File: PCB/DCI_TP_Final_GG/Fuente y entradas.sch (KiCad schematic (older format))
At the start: 0 parts

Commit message: Agrego esquematico de fuente (falta completar)
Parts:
- added C?: 47uF x 35V, symbol Device:CP
- added C? (x2): C, symbol Device:C
- added D?: LED, symbol Device:LED
- added J? (x2): Conn_01x02, symbol Connector_Generic:Conn_01x02
- added J? (x2): Conn_01x10, symbol Connector_Generic:Conn_01x10
- added JP?: Jumper, symbol Device:Jumper
- added R? (x4): R, symbol Device:R
- added U?: LM317_3PinPackage, symbol Regulator_Linear:LM317_3PinPackage
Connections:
- new net: R?.1, U?.1 (ADJ)
- new net: JP?.1, R?.1, R?.2
- new net: D?.2 (A), R?.2
- new net DIR-A: J?.8 (Pin_8)
- new net DIR-B: J?.8 (Pin_8)
- new net ENA-A: J?.5 (Pin_5)
- new net ENA-B: J?.5 (Pin_5)
- new net GND: C?.2, C?.2, C?.2, D?.1 (K), J?.1 (Pin_1), J?.1 (Pin_1), J?.1 (Pin_1), J?.2 (Pin_2), JP?.2, R?.2, R?.2
- new net MS1-A: J?.7 (Pin_7)
- new net MS1-B: J?.7 (Pin_7)
- new net MS2-A: J?.6 (Pin_6)
- new net MS2-B: J?.6 (Pin_6)
- new net PFD-A: J?.2 (Pin_2)
- new net PFD-B: J?.2 (Pin_2)
- new net RST-A: J?.4 (Pin_4)
- new net RST-B: J?.4 (Pin_4)
- new net SLEEP-A: J?.3 (Pin_3)
- new net SLEEP-B: J?.3 (Pin_3)
- new net STEP-A: J?.9 (Pin_9)
- new net STEP-B: J?.9 (Pin_9)
- new net VCC: C?.1, J?.1 (Pin_1), J?.10 (Pin_10), J?.10 (Pin_10), R?.1, R?.1, U?.2 (VO)
- new net VDD: C?.1, C?.1, J?.2 (Pin_2), U?.3 (VI)

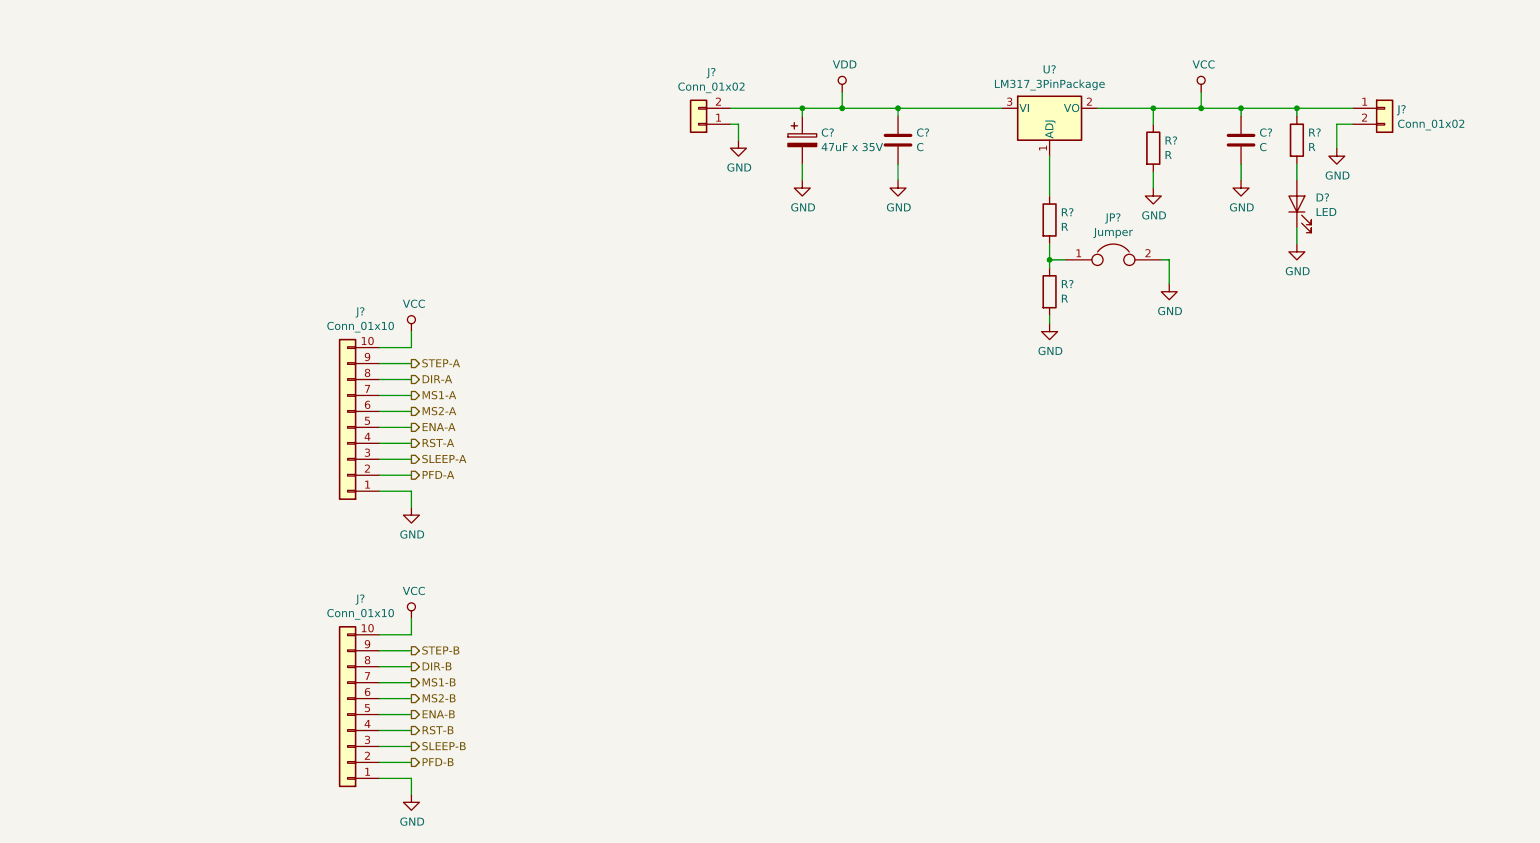
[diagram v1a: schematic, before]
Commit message: Hoja de fuente y conectores completa.
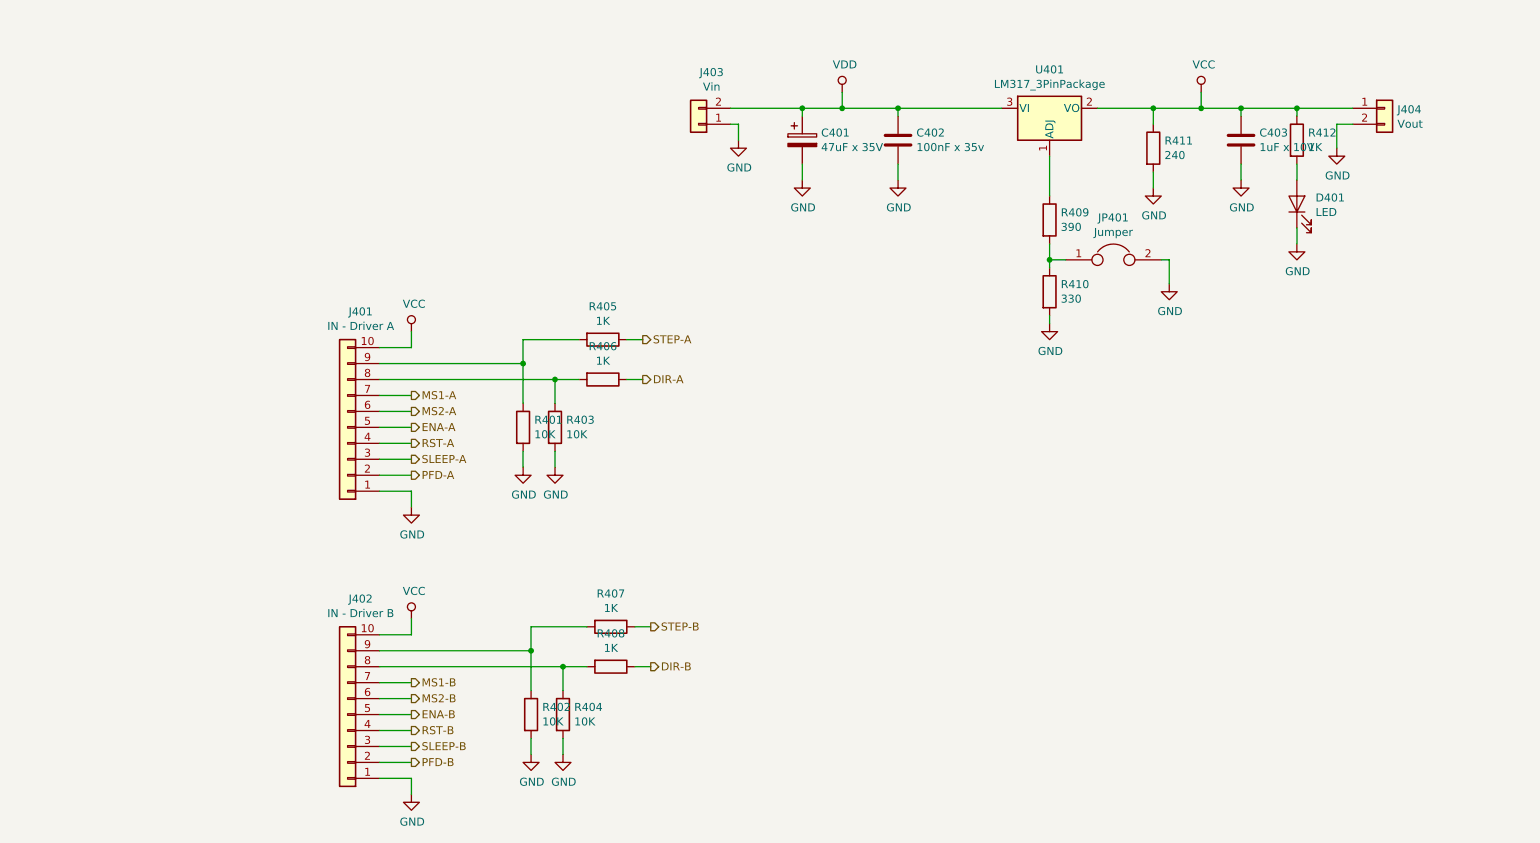
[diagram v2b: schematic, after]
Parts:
- added R401, R402, R403, R404: 10K, Resistor_SMD:R_0805_2012Metric, symbol Device:R
- added R405, R406, R407, R408: 1K, Resistor_SMD:R_0805_2012Metric, symbol Device:R
- C401: renamed from C?; footprint (none) -> Capacitor_THT:CP_Radial_D5.0mm_P2.00mm
- C402: renamed from C?; value C -> 100nF x 35v; footprint (none) -> Capacitor_SMD:C_0805_2012Metric
- C403: renamed from C?; value C -> 1uF x 10V; footprint (none) -> Capacitor_SMD:C_0805_2012Metric; Descripcion (none) -> C0805C105Z8VACTU
- D401: renamed from D?; footprint (none) -> LED_THT:LED_D3.0mm
- J401: renamed from J?; value Conn_01x10 -> IN - Driver A; footprint (none) -> Connector_PinHeader_2.54mm:PinHeader_1x10_P2.54mm_Vertical
- J402: renamed from J?; value Conn_01x10 -> IN - Driver B; footprint (none) -> Connector_PinHeader_2.54mm:PinHeader_1x10_P2.54mm_Vertical
- J403: renamed from J?; value Conn_01x02 -> Vin; footprint (none) -> TerminalBlock:TerminalBlock_Altech_AK300-2_P5.00mm
- J404: renamed from J?; value Conn_01x02 -> Vout; footprint (none) -> Connector_PinHeader_2.54mm:PinHeader_1x02_P2.54mm_Vertical
- JP401: renamed from JP?; footprint (none) -> Resistor_SMD:R_0805_2012Metric
- R409: renamed from R?; value R -> 390; footprint (none) -> Resistor_SMD:R_0805_2012Metric
- R410: renamed from R?; value R -> 330; footprint (none) -> Resistor_SMD:R_0805_2012Metric
- R411: renamed from R?; value R -> 240; footprint (none) -> Resistor_SMD:R_0805_2012Metric
- R412: renamed from R?; value R -> 1K; footprint (none) -> Resistor_SMD:R_0805_2012Metric
- U401: renamed from U?; footprint (none) -> Package_TO_SOT_SMD:SOT-223-3_TabPin2
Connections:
- net DIR-A: now also R406.1; no longer J401.8 (Pin_8)
- net DIR-B: now also R408.1; no longer J402.8 (Pin_8)
- net GND: now also R401.2, R402.2, R403.2, R404.2
- net STEP-A: now also R405.1; no longer J401.9 (Pin_9)
- net STEP-B: now also R407.1; no longer J402.9 (Pin_9)
- new net: J401.8 (Pin_8), R403.1, R406.2
- new net: J401.9 (Pin_9), R401.1, R405.2
- new net: J402.8 (Pin_8), R404.1, R408.2
- new net: J402.9 (Pin_9), R402.1, R407.2

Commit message: Se completo el esquematico y documentación. El esquematico esta listo para una primera revisión.
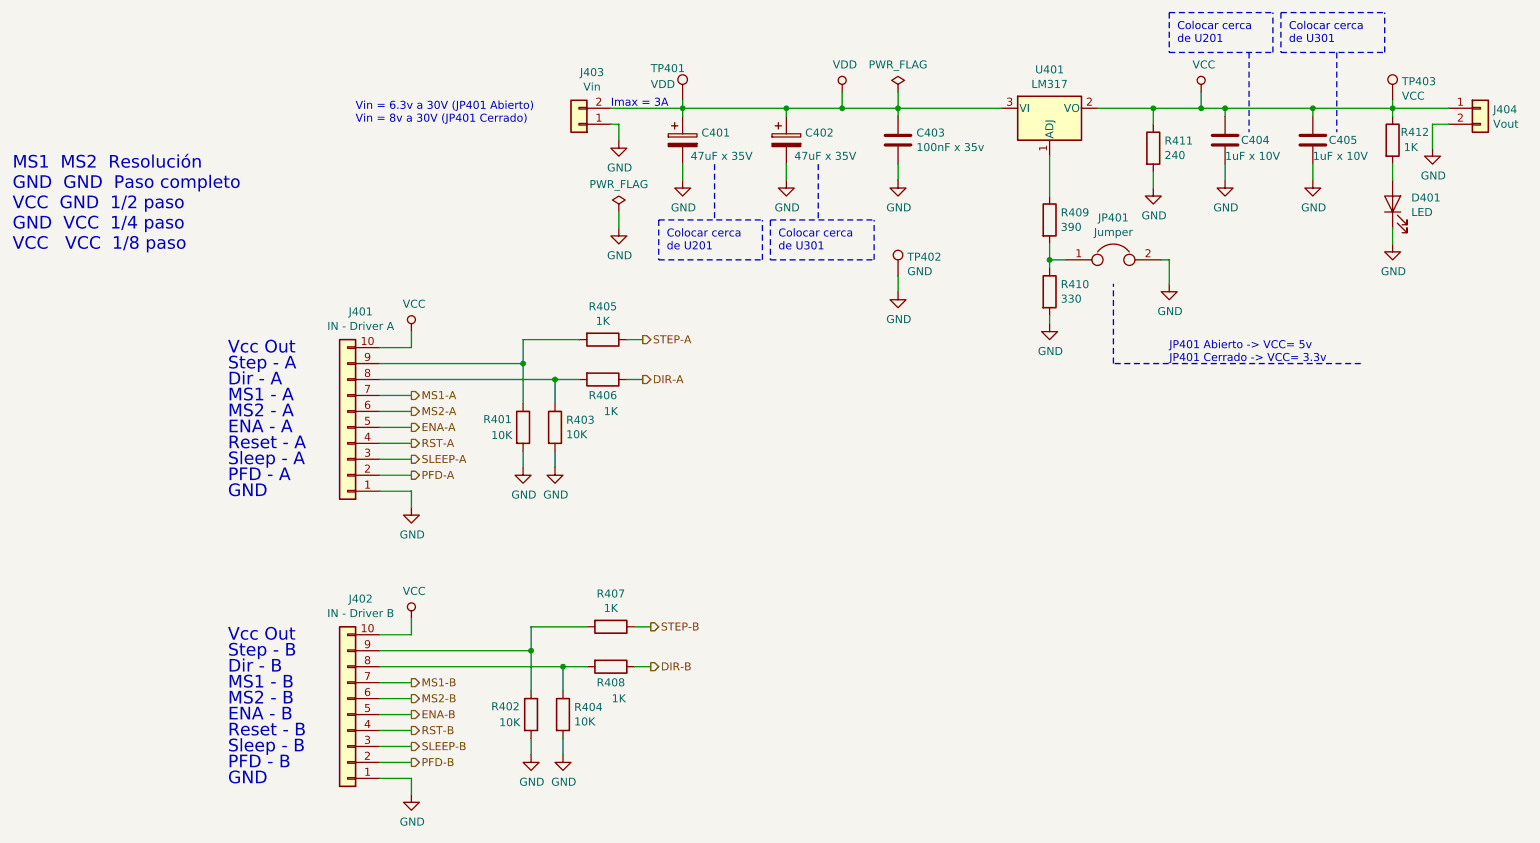
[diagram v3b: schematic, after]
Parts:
- added C402: 47uF x 35V, Capacitor_THT:CP_Radial_D5.0mm_P2.00mm, symbol Device:CP
- added C405: 1uF x 10V, Capacitor_SMD:C_0805_2012Metric, symbol Device:C
- added TP401: VDD, symbol Connector:TestPoint
- added TP402: GND, symbol Connector:TestPoint
- added TP403: VCC, symbol Connector:TestPoint
- U401: value LM317_3PinPackage -> LM317
- renumbered C402 to C403, C403 to C404
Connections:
- net GND: now also C402.2, C405.2, TP402.1
- net VCC: now also C405.1, TP403.1
- net VDD: now also C402.1, TP401.1
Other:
- note added: "Colocar cerca\nde U201"
- note added: "Colocar cerca\nde U301\n"
- note added: "Dir - A\n"
- note added: "Dir - B"
- note added: "ENA - A\n"
- note added: "ENA - B"
- note added: "GND"
- note added: "Imax = 3A"
- note added: "JP401 Abierto -> VCC= 5v\nJP401 Cerrado -> VCC= 3.3v"
- note added: "MS1 - A"
- note added: "MS1 - B"
- note added: "MS1 MS2 Resolución\nGND GND Paso completo\nVCC GND 1/2 paso\nGND VCC 1/4 paso\nVCC VCC 1/8 paso"
- note added: "MS2 - A\n"
- note added: "MS2 - B"
- note added: "PFD - A\n"
- note added: "PFD - B"
- note added: "Reset - A"
- note added: "Reset - B"
- note added: "Sleep - A\n"
- note added: "Sleep - B"
- note added: "Step - A"
- note added: "Step - B"
- note added: "Vcc Out"
- note added: "Vin = 6.3v a 30V (JP401 Abierto)\nVin = 8v a 30V (JP401 Cerrado)"
- moved on the sheet: C401, C404, D401, J403, J404, R412

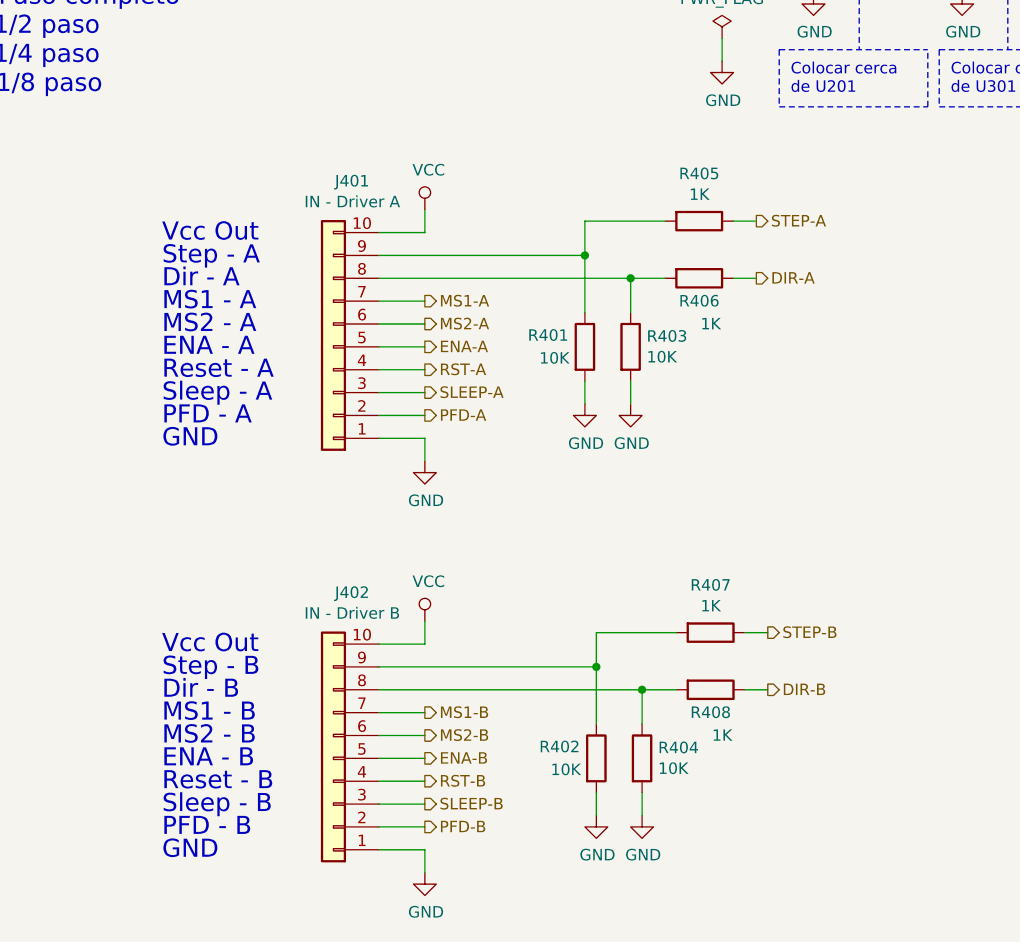
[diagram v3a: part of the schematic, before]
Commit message: Inicio etapa de desarrollo de PCB, agrego biblioteca de borneras
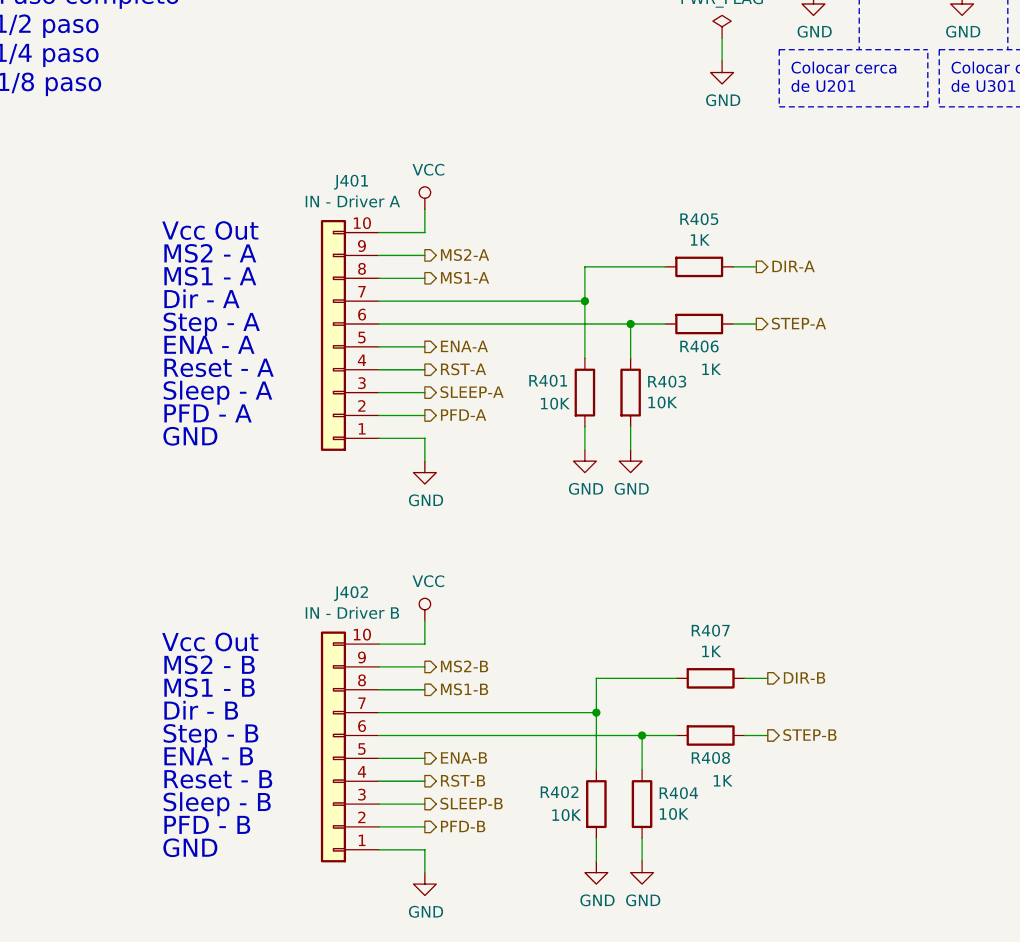
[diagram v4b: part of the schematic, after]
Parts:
- TP401, TP402, TP403: footprint (none) -> TestPoint:TestPoint_Pad_D2.0mm
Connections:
- net DIR-A: now also R405.1; no longer R406.1
- net DIR-B: now also R407.1; no longer R408.1
- net MS1-A: now also J401.8 (Pin_8); no longer J401.7 (Pin_7)
- net MS1-B: now also J402.8 (Pin_8); no longer J402.7 (Pin_7)
- net MS2-A: now also J401.9 (Pin_9); no longer J401.6 (Pin_6)
- net MS2-B: now also J402.9 (Pin_9); no longer J402.6 (Pin_6)
- net STEP-A: now also R406.1; no longer R405.1
- net STEP-B: now also R408.1; no longer R407.1
- net at R403.1, R406.2: now also J401.6 (Pin_6); no longer J401.8 (Pin_8)
- net at R401.1, R405.2: now also J401.7 (Pin_7); no longer J401.9 (Pin_9)
- net at R404.1, R408.2: now also J402.6 (Pin_6); no longer J402.8 (Pin_8)
- net at R402.1, R407.2: now also J402.7 (Pin_7); no longer J402.9 (Pin_9)
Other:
- moved on the sheet: R401, R402, R403, R404, R405, R406, R407, R408

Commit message: Avance en routeo
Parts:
- J403: footprint TerminalBlock:TerminalBlock_Altech_AK300-2_P5.00mm -> TerminalBlock_Phoenix:TerminalBlock_Phoenix_MKDS-1,5-2_1x02_P5.00mm_Horizontal
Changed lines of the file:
@@
 F 0 "J403" H 4368 1875 50  0000 C CNN
 F 1 "Vin" H 4368 1966 50  0000 C CNN
-F 2 "TerminalBlock:TerminalBlock_Altech_AK300-2_P5.00mm" H 4450 2200 50  0001 C CNN
+F 2 "TerminalBlock_Phoenix:TerminalBlock_Phoenix_MKDS-1,5-2_1x02_P5.00mm_Horizontal" H 4450 2200 50  0001 C CNN
 F 3 "~" H 4450 2200 50  0001 C CNN
 	1    4450 2200
